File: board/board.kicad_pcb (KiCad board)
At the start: 2 copper layers, 21 x 13 mm, 1 part

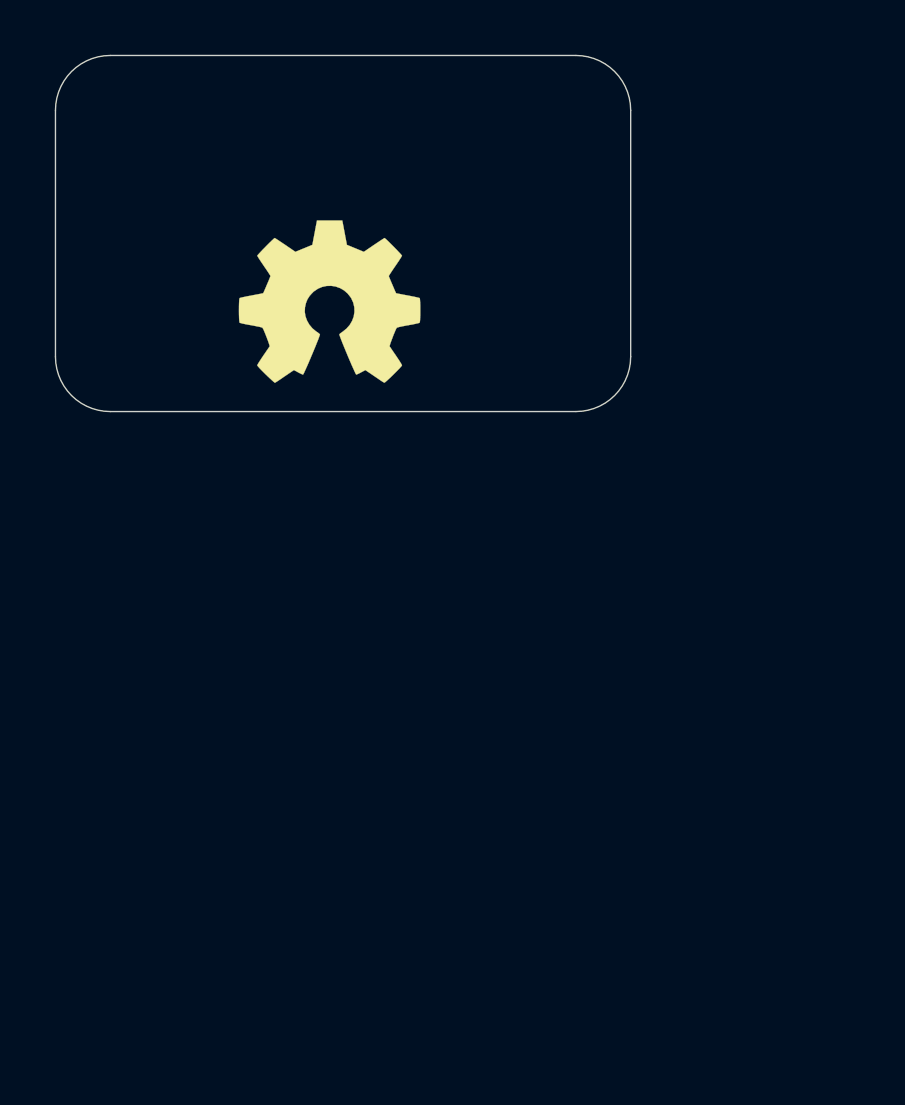
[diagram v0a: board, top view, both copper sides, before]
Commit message: Add footprint, schema, 3D Model | Start circuit design
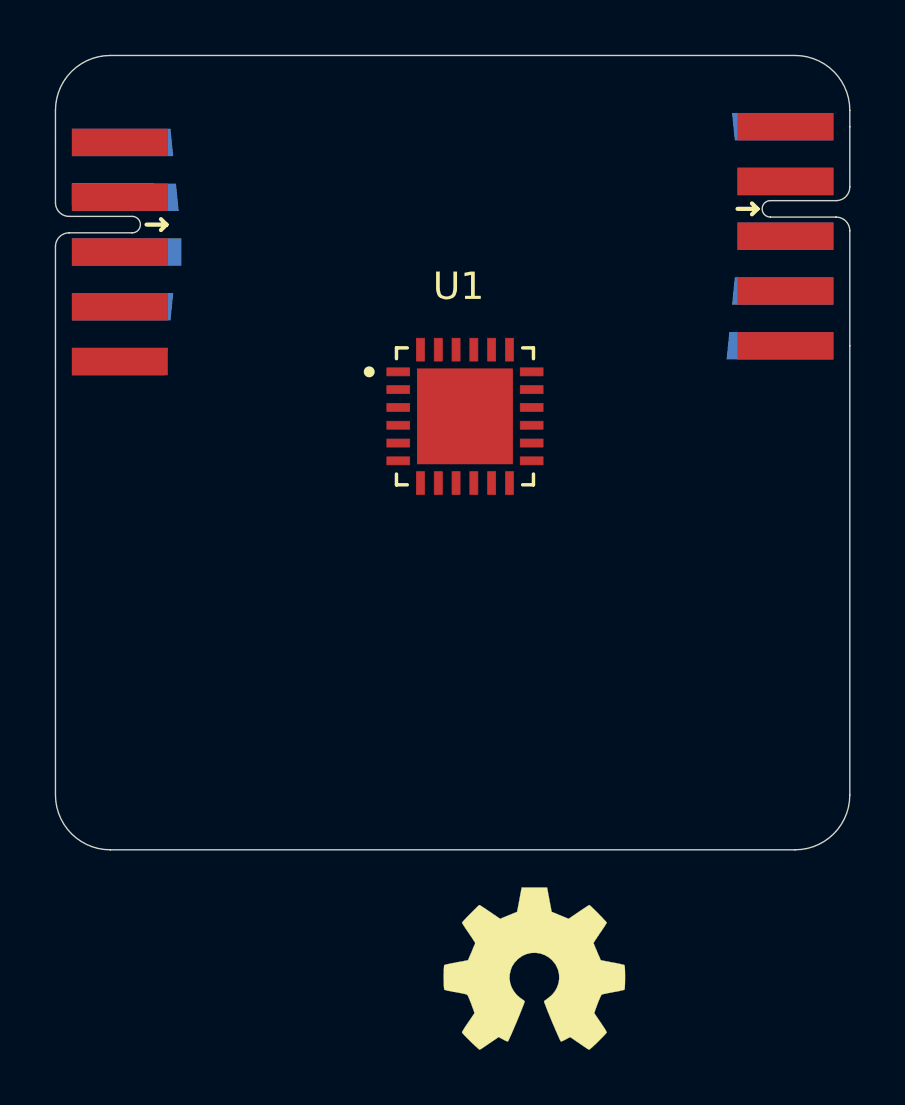
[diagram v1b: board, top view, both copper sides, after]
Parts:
- added J1: 001_I2C, on_edge:on_edge_2x05_device, F.Cu at (140.0, 97.2)
- added J2: 011_GPIO, on_edge:on_edge_2x05_host, F.Cu at (169.0, 96.6)
- added U1: ALED7709ATR, led_treiber_edgy:QFN65P500X500X90-25N, F.Cu at (154.9, 103.2)
- moved LOGO1 25.5 mm to (157.5, 123.3)
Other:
- board size 21 x 13 mm -> 29 x 29 mm
